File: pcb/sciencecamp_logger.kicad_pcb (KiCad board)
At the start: 2 copper layers, 97 x 46 mm, 33 parts, among them J1 1-Wire, J2 HC-SR04, J3 OLED, J4 Micro_SD_Card_Det, SW1 OFF/ON, SW2 action, U1 74LVC125, U2 AMS1117-3.3

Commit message: Small fixes
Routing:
- net GND: track 44.3 -> 53.8 mm
- net SPI_SCK: track 53.2 -> 50.6 mm
- net Net-(BT1-Pad1): track 45.8 -> 44.6 mm
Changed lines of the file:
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@@
     (thickness 1.6)
     (drawings 29)
-    (tracks 399)
+    (tracks 403)
     (zones 0)
     (modules 33)
@@
       (effects (font (size 1 1) (thickness 0.15)))
     )
-    (fp_text value 47k (at 2.54 1.92) (layer F.Fab)
+    (fp_text value 47k (at 2.54 1.92) (layer F.SilkS)
       (effects (font (size 1 1) (thickness 0.15)))
     )
@@
   (segment (start 184.375 118.775) (end 184.375 114.5) (width 1) (layer F.Cu) (net 1))
   (segment (start 185.849999 117.952931) (end 185.849999 117.702931) (width 1) (layer B.Cu) (net 1))
-  (segment (start 196.055013 95.900011) (end 173.515011 95.900011) (width 1) (layer B.Cu) (net 1))
   (segment (start 185.849999 117.202931) (end 188.05293 115) (width 1) (layer B.Cu) (net 1))
-  (segment (start 173.515011 95.900011) (end 169.799999 92.184999) (width 1) (layer B.Cu) (net 1))
-  (segment (start 206.5 106.344998) (end 196.055013 95.900011) (width 1) (layer B.Cu) (net 1))
   (segment (start 185.849999 117.452931) (end 185.849999 117.202931) (width 1) (layer B.Cu) (net 1))
   (segment (start 185.849999 118.202931) (end 185.849999 117.952931) (width 1) (layer B.Cu) (net 1))
   (segment (start 195.010051 115) (end 196 115) (width 1) (layer B.Cu) (net 1))
-  (segment (start 190.05293 113) (end 202 113) (width 1) (layer B.Cu) (net 1))
   (segment (start 188.05293 115) (end 195.010051 115) (width 1) (layer B.Cu) (net 1))
-  (segment (start 206.5 108.5) (end 206.5 106.344998) (width 1) (layer B.Cu) (net 1))
-  (segment (start 202 113) (end 206.5 108.5) (width 1) (layer B.Cu) (net 1))
-  (segment (start 185.849999 117.202931) (end 190.05293 113) (width 1) (layer B.Cu) (net 1))
   (segment (start 185.849999 118.650001) (end 185.849999 118.452931) (width 1) (layer B.Cu) (net 1))
   (segment (start 185.849999 117.702931) (end 185.849999 117.452931) (width 1) (layer B.Cu) (net 1))
   (segment (start 185.849999 118.452931) (end 185.849999 118.202931) (width 1) (layer B.Cu) (net 1))
+  (segment (start 173.515011 95.900011) (end 169.799999 92.184999) (width 1) (layer B.Cu) (net 1))
+  (segment (start 206.5 106.43728) (end 195.962731 95.900011) (width 1) (layer B.Cu) (net 1))
+  (segment (start 185.849999 117.202931) (end 190.05293 113) (width 1) (layer B.Cu) (net 1))
+  (segment (start 195.962731 95.900011) (end 173.515011 95.900011) (width 1) (layer B.Cu) (net 1))
+  (segment (start 190.05293 113) (end 202 113) (width 1) (layer B.Cu) (net 1))
+  (segment (start 202 113) (end 206.5 108.5) (width 1) (layer B.Cu) (net 1))
   (segment (start 169.799999 92.184999) (end 169 91.385) (width 1) (layer B.Cu) (net 1))
+  (segment (start 206.5 108.5) (end 206.5 106.43728) (width 1) (layer B.Cu) (net 1))
   (via (at 174.25 83.75) (size 0.8) (drill 0.4) (layers F.Cu B.Cu) (net 2))
   (via (at 174.25 82.5) (size 0.8) (drill 0.4) (layers F.Cu B.Cu) (net 2))
@@
   (via (at 188.25 80.5) (size 0.8) (drill 0.4) (layers F.Cu B.Cu) (net 2))
   (via (at 187.25 80.5) (size 0.8) (drill 0.4) (layers F.Cu B.Cu) (net 2))
+  (segment (start 200.7 98.5) (end 201.675 98.5) (width 0.25) (layer F.Cu) (net 2))
+  (segment (start 201.675 98.5) (end 202.75 98.5) (width 0.25) (layer F.Cu) (net 2))
+  (segment (start 202.75 98.5) (end 203 98.75) (width 0.25) (layer F.Cu) (net 2))
+  (segment (start 203 98.75) (end 203 103.5) (width 0.25) (layer F.Cu) (net 2))
+  (segment (start 203 103.5) (end 202.75 103.75) (width 0.25) (layer F.Cu) (net 2))
+  (segment (start 202.75 103.75) (end 200.75 103.75) (width 0.25) (layer F.Cu) (net 2))
   (segment (start 160 97.79) (end 131.96 97.79) (width 1) (layer B.Cu) (net 5))
   (segment (start 126.75 103) (end 117.75 103) (width 1) (layer B.Cu) (net 5))
@@
   (segment (start 200.985001 117.235001) (end 187.514999 117.235001) (width 1) (layer B.Cu) (net 24))
   (segment (start 200.985001 117.235001) (end 208.200009 110.019993) (width 1) (layer B.Cu) (net 24))
-  (segment (start 200.170003 118.049999) (end 200.985001 117.235001) (width 1) (layer B.Cu) (net 24))
   (segment (start 187.1 117.65) (end 187.1 119.5) (width 1) (layer B.Cu) (net 24))
   (segment (start 187.514999 117.235001) (end 187.1 117.65) (width 1) (layer B.Cu) (net 24))
@@
   (segment (start 204.5 91.445) (end 204.56 91.385) (width 0.25) (layer F.Cu) (net 26))
   (segment (start 204.5 93.375) (end 204.5 91.445) (width 0.25) (layer F.Cu) (net 26))
-  (segment (start 205.359999 90.585001) (end 205.359999 89.109999) (width 0.25) (layer B.Cu) (net 26))
-  (segment (start 204.56 91.385) (end 205.359999 90.585001) (width 0.25) (layer B.Cu) (net 26))
   (via (at 180.5 93.5) (size 0.8) (drill 0.4) (layers F.Cu B.Cu) (net 26))
   (segment (start 180.5 85.5) (end 180.5 93.5) (width 0.25) (layer B.Cu) (net 26))
@@
   (segment (start 198.35 88.65) (end 198.35 88.15) (width 0.25) (layer F.Cu) (net 30))
   (segment (start 198.35 88.15) (end 199.25 87.25) (width 0.25) (layer F.Cu) (net 30))
-  (segment (start 204.000928 102.375928) (end 204.5 102.875) (width 0.25) (layer F.Cu) (net 30))
-  (segment (start 203.574999 101.949999) (end 204.000928 102.375928) (width 0.25) (layer F.Cu) (net 30))
-  (segment (start 203.574999 97.145001) (end 203.574999 101.949999) (width 0.25) (layer F.Cu) (net 30))
   (segment (start 198.35 88.65) (end 198.35 91.920002) (width 0.25) (layer F.Cu) (net 30))
   (segment (start 200.1 93.5) (end 200.014999 93.585001) (width 0.25) (layer F.Cu) (net 30))
   (segment (start 201.325 93.5) (end 200.1 93.5) (width 0.25) (layer F.Cu) (net 30))
   (segment (start 198.35 91.920002) (end 200.014999 93.585001) (width 0.25) (layer F.Cu) (net 30))
+  (segment (start 203.574999 97.145001) (end 203.574999 101.949999) (width 0.25) (layer F.Cu) (net 30))
+  (segment (start 204.000928 102.375928) (end 204.5 102.875) (width 0.25) (layer F.Cu) (net 30))
   (segment (start 200.014999 93.585001) (end 203.574999 97.145001) (width 0.25) (layer F.Cu) (net 30))
+  (segment (start 203.574999 101.949999) (end 204.000928 102.375928) (width 0.25) (layer F.Cu) (net 30))
   (segment (start 198.065001 89.565001) (end 195.5 87) (width 0.25) (layer B.Cu) (net 31))
   (segment (start 198.065001 92.369314) (end 198.065001 89.565001) (width 0.25) (layer B.Cu) (net 31))
@@
   (segment (start 198 93) (end 198 92.434315) (width 0.25) (layer B.Cu) (net 31))
   (via (at 198 93) (size 0.8) (drill 0.4) (layers F.Cu B.Cu) (net 31))
-  (segment (start 198 93) (end 198.75 93) (width 0.25) (layer F.Cu) (net 31))
-  (segment (start 198.75 93) (end 202.25 96.5) (width 0.25) (layer F.Cu) (net 31))
-  (segment (start 201.675 97.2) (end 200.7 97.2) (width 0.25) (layer F.Cu) (net 31))
-  (segment (start 202.25 96.625) (end 201.675 97.2) (width 0.25) (layer F.Cu) (net 31))
-  (segment (start 202.25 96.5) (end 202.25 96.625) (width 0.25) (layer F.Cu) (net 31))
+  (segment (start 198.565685 93) (end 198 93) (width 0.25) (layer F.Cu) (net 31))
+  (segment (start 202 96.314998) (end 198.685002 93) (width 0.25) (layer F.Cu) (net 31))
+  (segment (start 198.685002 93) (end 198.565685 93) (width 0.25) (layer F.Cu) (net 31))
+  (segment (start 201.675 97.2) (end 202 96.875) (width 0.25) (layer F.Cu) (net 31))
+  (segment (start 202 96.875) (end 202 96.314998) (width 0.25) (layer F.Cu) (net 31))
+  (segment (start 200.7 97.2) (end 201.675 97.2) (width 0.25) (layer F.Cu) (net 31))
   (segment (start 196.15 89.6) (end 195.814999 89.935001) (width 0.25) (layer F.Cu) (net 32))
   (segment (start 195.814999 89.935001) (end 195.814999 92.827563) (width 0.25) (layer F.Cu) (net 32))
@@
   (segment (start 198.25 95.262564) (end 195.814999 92.827563) (width 0.25) (layer F.Cu) (net 32))
   (segment (start 198.25 97.675) (end 198.25 95.262564) (width 0.25) (layer F.Cu) (net 32))
-  (via (at 202.5 100.5) (size 0.8) (drill 0.4) (layers F.Cu B.Cu) (net 33))
-  (segment (start 202 102.875) (end 202 101) (width 0.25) (layer F.Cu) (net 33))
-  (segment (start 202 101) (end 202.5 100.5) (width 0.25) (layer F.Cu) (net 33))
   (via (at 202.25 97.75) (size 0.8) (drill 0.4) (layers F.Cu B.Cu) (net 33))
   (segment (start 200.8 97.75) (end 200.7 97.85) (width 0.25) (layer F.Cu) (net 33))
   (segment (start 202.25 97.75) (end 200.8 97.75) (width 0.25) (layer F.Cu) (net 33))
-  (segment (start 202.975002 98.475002) (end 202.649999 98.149999) (width 0.25) (layer B.Cu) (net 33))
-  (segment (start 202.649999 98.149999) (end 202.25 97.75) (width 0.25) (layer B.Cu) (net 33))
-  (segment (start 202.975002 100.024998) (end 202.975002 98.475002) (width 0.25) (layer B.Cu) (net 33))
-  (segment (start 202.5 100.5) (end 202.975002 100.024998) (width 0.25) (layer B.Cu) (net 33))
+  (segment (start 202 100.864845) (end 202.27499 100.589855) (width 0.25) (layer F.Cu) (net 33))
+  (segment (start 202.975002 98.475002) (end 202.975002 99.889843) (width 0.25) (layer B.Cu) (net 33))
+  (segment (start 202.25 97.75) (end 202.975002 98.475002) (width 0.25) (layer B.Cu) (net 33))
+  (segment (start 202.975002 99.889843) (end 202.674989 100.189856) (width 0.25) (layer B.Cu) (net 33))
+  (via (at 202.27499 100.589855) (size 0.8) (drill 0.4) (layers F.Cu B.Cu) (net 33))
+  (segment (start 202 102.875) (end 202 100.864845) (width 0.25) (layer F.Cu) (net 33))
+  (segment (start 202.674989 100.189856) (end 202.27499 100.589855) (width 0.25) (layer B.Cu) (net 33))
   (via (at 202.75 95) (size 0.8) (drill 0.4) (layers F.Cu B.Cu) (net 34))
   (segment (start 204.5 95.125) (end 202.875 95.125) (width 0.25) (layer F.Cu) (net 34))

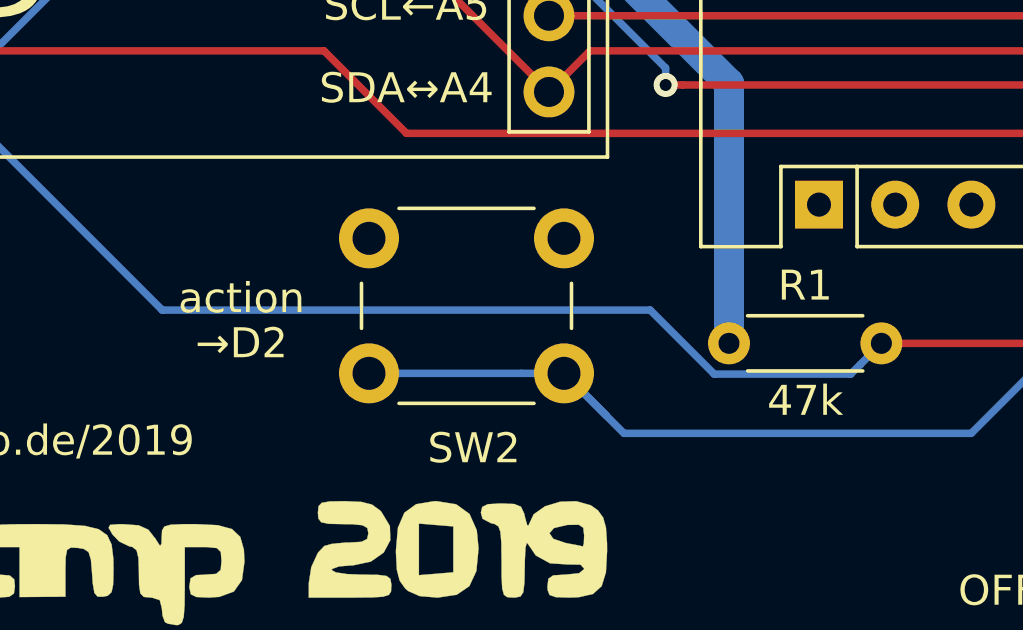
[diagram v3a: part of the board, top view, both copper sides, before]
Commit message: FIX: correct label and location
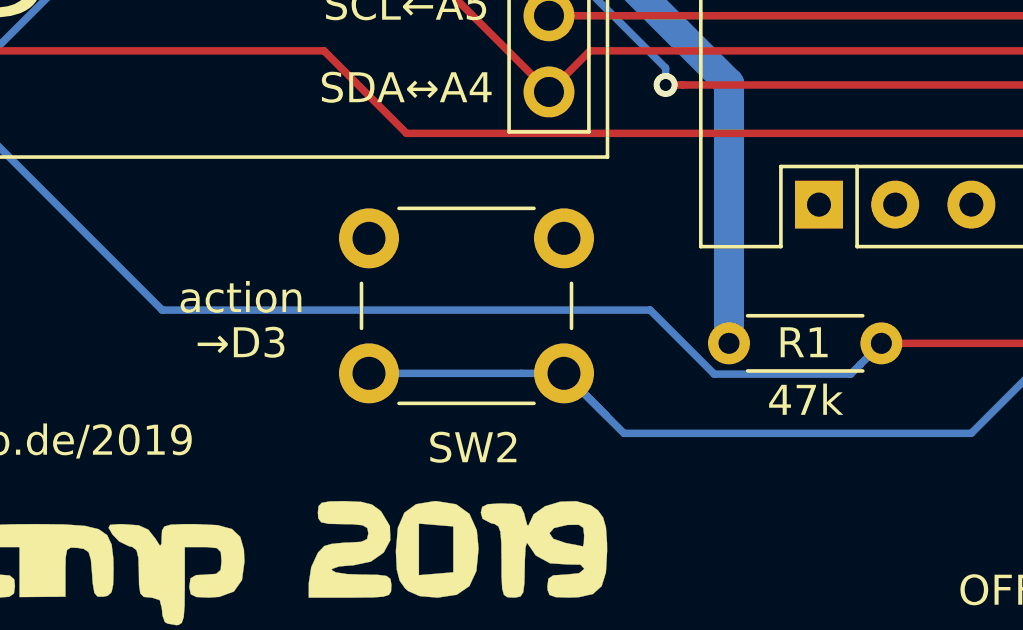
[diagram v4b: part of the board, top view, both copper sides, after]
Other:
- board text added: "→D3"
- board text removed: "→D2"
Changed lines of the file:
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@@
     (descr "Resistor, Axial_DIN0204 series, Axial, Horizontal, pin pitch=5.08mm, 0.167W, length*diameter=3.6*1.6mm^2, http://cdn-reichelt.de/documents/datenblatt/B400/1_4W%23YAG.pdf")
     (tags "Resistor Axial_DIN0204 series Axial Horizontal pin pitch 5.08mm 0.167W length 3.6mm diameter 1.6mm")
-    (fp_text reference R1 (at 2.54 -1.92) (layer F.SilkS)
+    (fp_text reference R1 (at 2.5 0) (layer F.SilkS)
       (effects (font (size 1 1) (thickness 0.15)))
     )
@@
     (effects (font (size 1 1) (thickness 0.15)))
   )
-  (gr_text →D2 (at 149.75 111.25) (layer F.SilkS)
+  (gr_text →D3 (at 149.75 111.25) (layer F.SilkS)
     (effects (font (size 1 1) (thickness 0.15)))
   )

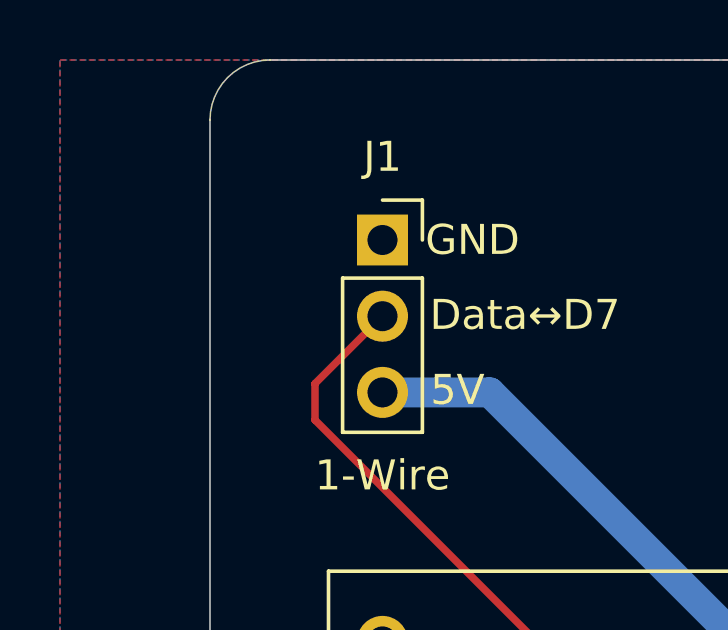
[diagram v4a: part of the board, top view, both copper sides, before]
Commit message: ADD: strain relief for one-wire sensor
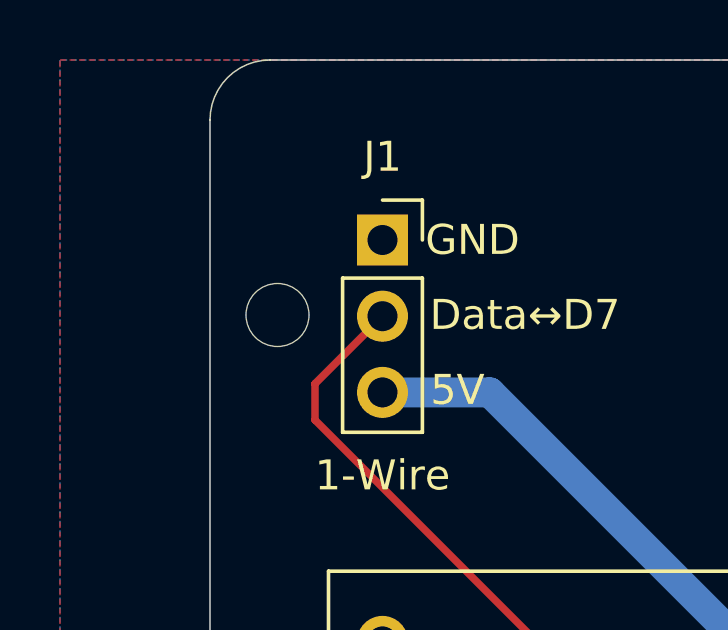
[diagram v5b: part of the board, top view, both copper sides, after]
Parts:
- added REF**: MountingHole_2.1mm, MountingHole:MountingHole_2.1mm, F.Cu at (114.2, 84.5)
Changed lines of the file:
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@@
     (tracks 403)
     (zones 0)
-    (modules 33)
+    (modules 34)
     (nets 42)
   )
@@
     (add_net SPI_SCK)
   )
+  (module MountingHole:MountingHole_2.1mm locked (layer F.Cu)
+    (at 114.25 84.5)
+    (descr "Mounting Hole 2.1mm, no annular")
+    (tags "mounting hole 2.1mm no annular")
+    (attr virtual)
+    (fp_text reference REF** (at 0 -3.2) (layer F.Fab)
+      (effects (font (size 1 1) (thickness 0.15)))
+    )
+    (fp_text value MountingHole_2.1mm (at 0 3.2) (layer F.Fab)
+      (effects (font (size 1 1) (thickness 0.15)))
+    )
+    (fp_circle (center 0 0) (end 2.35 0) (layer F.CrtYd) (width 0.05))
+    (fp_circle (center 0 0) (end 2.1 0) (layer Cmts.User) (width 0.15))
+    (fp_text user %R (at 0.3 0) (layer F.Fab)
+      (effects (font (size 1 1) (thickness 0.15)))
+    )
+    (pad "" np_thru_hole circle (at 0 0) (size 2.1 2.1) (drill 2.1) (layers *.Cu *.Mask))
+  )
   (module parts:SOFNG_TF-15_15 (layer F.Cu)

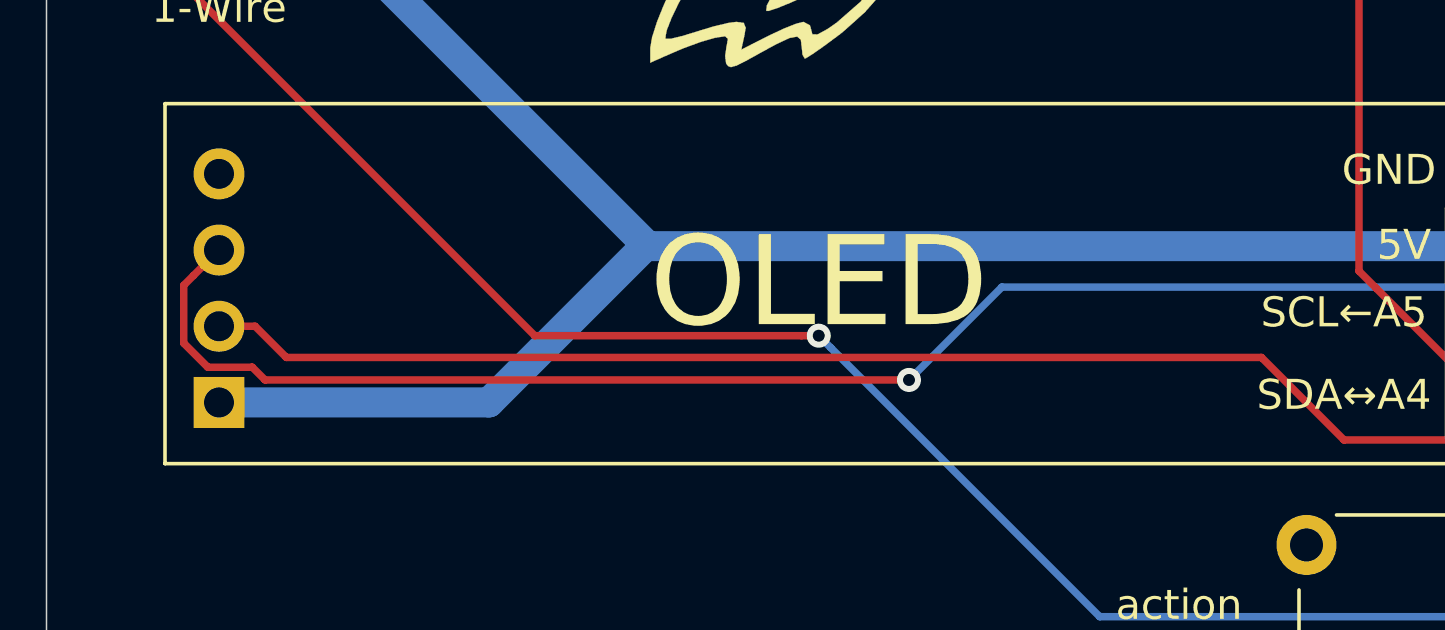
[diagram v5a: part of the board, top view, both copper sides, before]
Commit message: FIX: mixed up ultrasonic pins
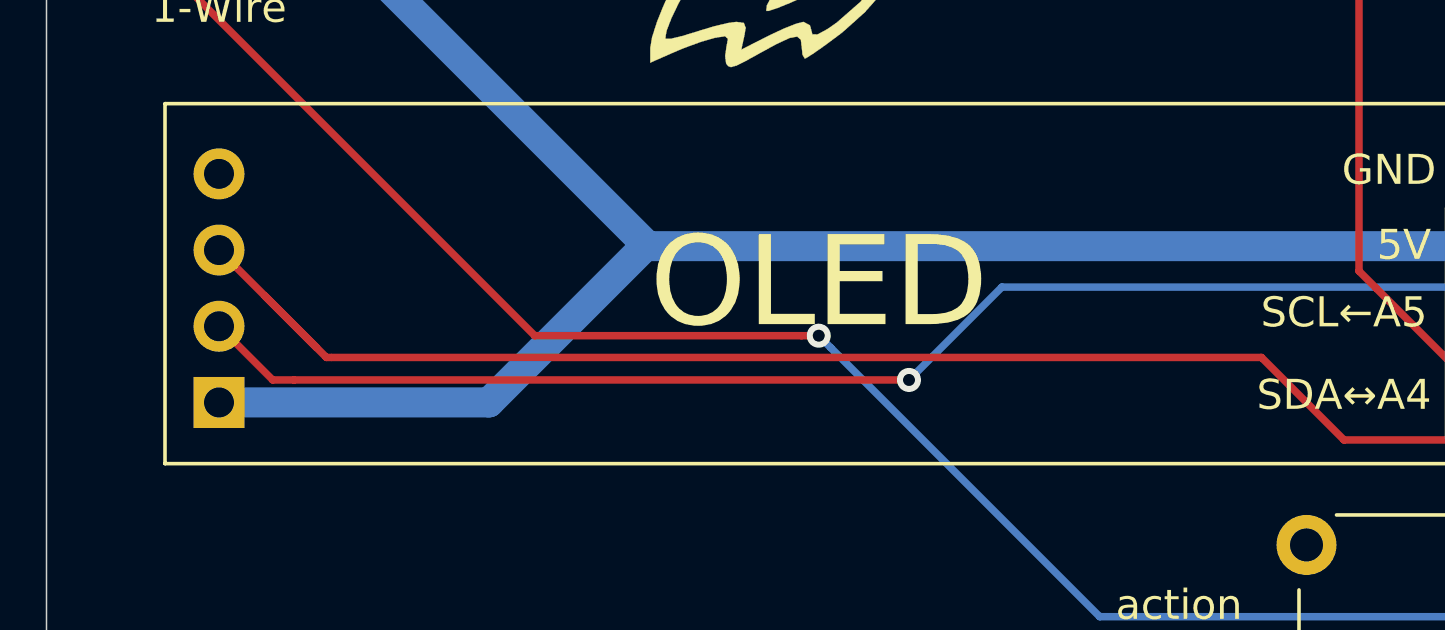
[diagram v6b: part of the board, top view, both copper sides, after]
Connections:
- A1 pad 5: Net-(A1-Pad5) -> /ECHO
- A1 pad 9: Net-(A1-Pad9) -> /TRIGGER
- J2 pad 2: Net-(A1-Pad5) -> /TRIGGER
- J2 pad 3: Net-(A1-Pad9) -> /ECHO
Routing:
- net Net-(A1-Pad9): track 81.6 -> 0.00 mm, vias 2 -> 0
- net /TRIGGER: track 0.00 -> 77.0 mm, vias 0 -> 2
- net /ECHO: track 0.00 -> 67.4 mm
- net Net-(A1-Pad5): track 64.0 -> 0.00 mm
